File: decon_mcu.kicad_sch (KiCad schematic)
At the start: 56 parts, among them J1 Conn_01x02, J10 Conn_01x04, J11 Conn_01x06, J12 Conn_01x06, J13 Conn_01x04, J14 Conn_01x16, J15 Conn_01x16, J16 Conn_01x16, J17 Conn_01x16, J18 Conn_01x04, J2 GPIO, J3 Conn_01x06, J4 Conn_01x06, J5 FLASH, J6 Conn_01x06, J7 Conn_01x05, J8 Conn_01x06, J9 Conn_01x06, SW1 SW_Push, SW2 SW_Push, U1 URB2405YMD-10WR3, U2 AZ1117-3.3, U3 STM32F401R_B-C_Tx, Y1 Crystal, Y2 Crystal_GND24

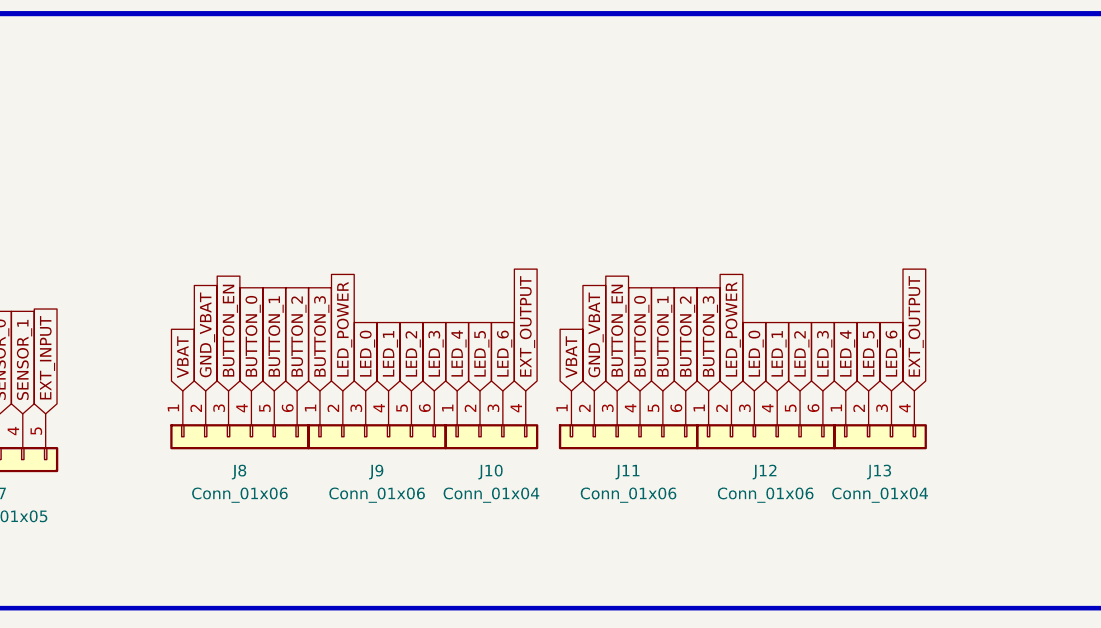
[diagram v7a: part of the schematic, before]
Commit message: modified:   DECON_Ctrl_Panel.kicad_pcb 	modified:   DECON_Ctrl_Panel.kicad_prl 	modified:   decon_mcu.kicad_sch
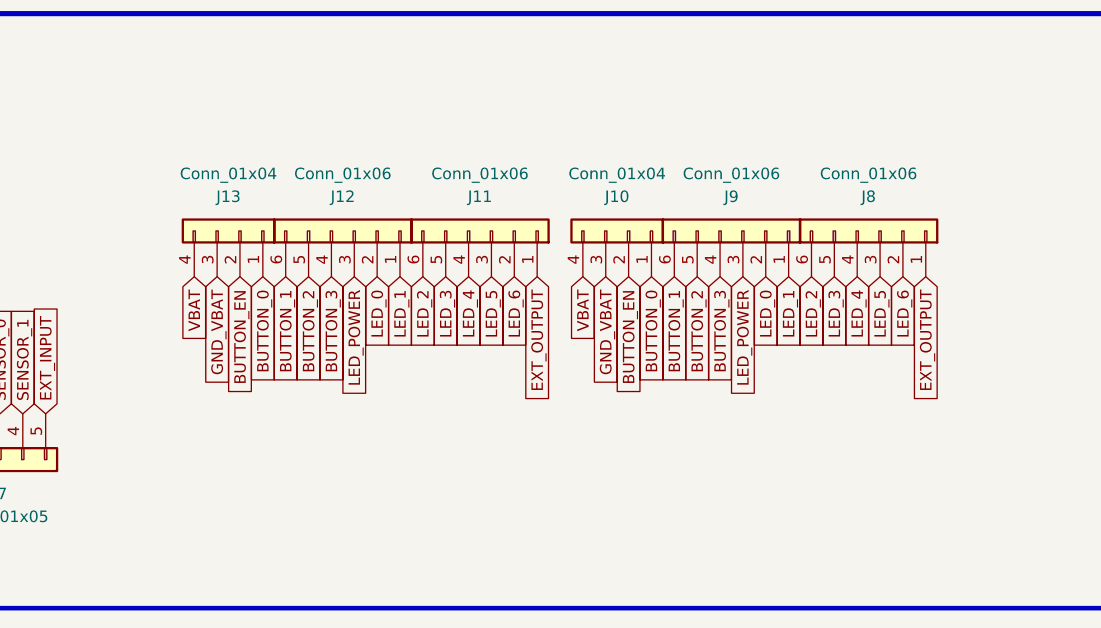
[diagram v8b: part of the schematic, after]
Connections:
- net BUTTON_0: now also J10.1 (Pin_1), J13.1 (Pin_1); no longer J11.4 (Pin_4), J8.4 (Pin_4)
- net BUTTON_1: now also J12.6 (Pin_6), J9.6 (Pin_6); no longer J11.5 (Pin_5), J8.5 (Pin_5)
- net BUTTON_2: now also J12.5 (Pin_5), J9.5 (Pin_5); no longer J11.6 (Pin_6), J8.6 (Pin_6)
- net BUTTON_3: now also J12.4 (Pin_4), J9.4 (Pin_4); no longer J12.1 (Pin_1), J9.1 (Pin_1)
- net BUTTON_EN: now also J10.2 (Pin_2), J13.2 (Pin_2); no longer J11.3 (Pin_3), J8.3 (Pin_3)
- net EXT_OUTPUT: now also J11.1 (Pin_1), J8.1 (Pin_1); no longer J10.4 (Pin_4), J13.4 (Pin_4)
- net GND_VBAT: now also J10.3 (Pin_3), J13.3 (Pin_3); no longer J11.2 (Pin_2), J8.2 (Pin_2)
- net LED_0: now also J12.2 (Pin_2), J9.2 (Pin_2); no longer J12.3 (Pin_3), J9.3 (Pin_3)
- net LED_1: now also J12.1 (Pin_1), J9.1 (Pin_1); no longer J12.4 (Pin_4), J9.4 (Pin_4)
- net LED_2: now also J11.6 (Pin_6), J8.6 (Pin_6); no longer J12.5 (Pin_5), J9.5 (Pin_5)
- net LED_3: now also J11.5 (Pin_5), J8.5 (Pin_5); no longer J12.6 (Pin_6), J9.6 (Pin_6)
- net LED_4: now also J11.4 (Pin_4), J8.4 (Pin_4); no longer J10.1 (Pin_1), J13.1 (Pin_1)
- net LED_5: now also J11.3 (Pin_3), J8.3 (Pin_3); no longer J10.2 (Pin_2), J13.2 (Pin_2)
- net LED_6: now also J11.2 (Pin_2), J8.2 (Pin_2); no longer J10.3 (Pin_3), J13.3 (Pin_3)
- net LED_POWER: now also J12.3 (Pin_3), J9.3 (Pin_3); no longer J12.2 (Pin_2), J9.2 (Pin_2)
- net VBAT: now also J10.4 (Pin_4), J13.4 (Pin_4); no longer J11.1 (Pin_1), J8.1 (Pin_1)
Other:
- moved on the sheet: J10, J11, J12, J13, J8, J9
